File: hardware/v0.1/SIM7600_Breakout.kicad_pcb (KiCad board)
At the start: 4 copper layers, 40 x 80 mm, 68 parts, among them J1 SIM8060-6-0-14-00-A, J2 2W Header, J3 MJ-3502N, J4 30W Header, J5 2137160001, J6 U.FL-R-SMT-1(01), J7 U.FL-R-SMT-1(01), J8 U.FL-R-SMT-1(01), Q1 MMBT3904L_RFG, U1 NVT2008PW_118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

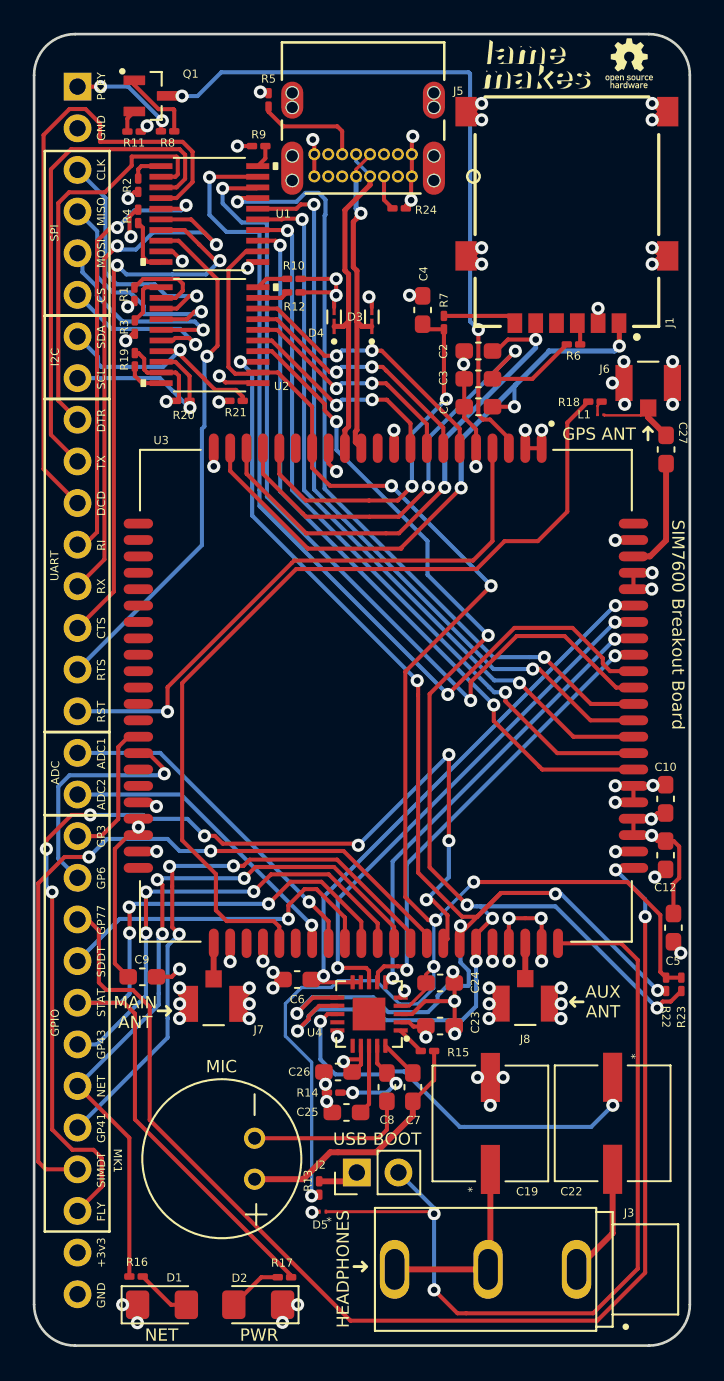
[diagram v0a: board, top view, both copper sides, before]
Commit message: Added project wide versioning, cleaned up & added PCB text
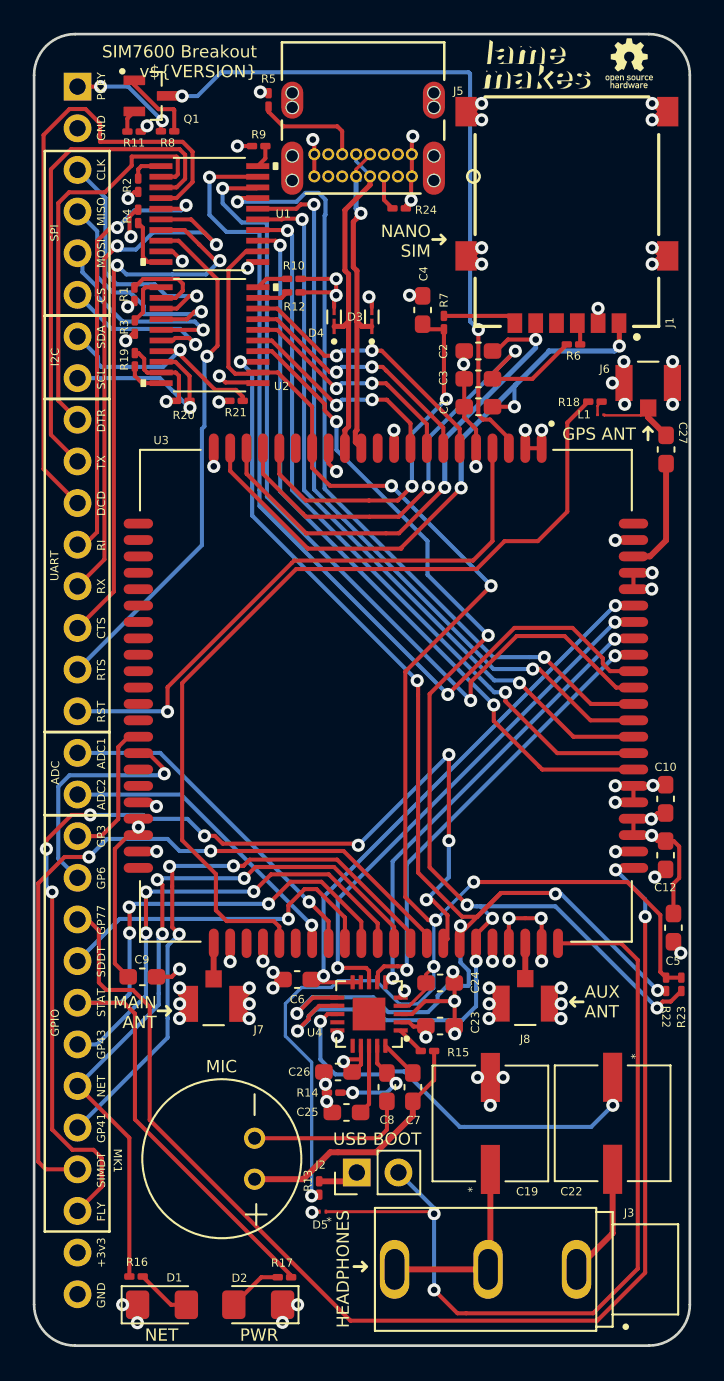
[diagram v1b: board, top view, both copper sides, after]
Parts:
- added G***: LOGO, sim7600_breakout:arrow, F.Cu at (143.7, 77.2)
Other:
- board text added: "NANO SIM"
- board text added: "SIM7600 Breakout v${VERSION}"
- board text removed: "SIM7600 Breakout Board"
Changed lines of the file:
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@@
 		)
 	)
+	(property "VERSION" "0.1")
 	(net 0 "")
 	(net 1 "/SIM_VCC")
@@
 		(at 126.13 68.44)
 		(property "Reference" "Q1"
-			(at 2.42 -1.34 0)
+			(at 2.47 1.41 0)
 			(unlocked yes)
 			(layer "F.SilkS")
@@
 		)
 	)
+	(footprint "sim7600_breakout:arrow"
+		(layer "F.Cu")
+		(at 143.7 77.2)
+		(property "Reference" "G***"
+			(at 0 -1.275 0)
+			(unlocked yes)
+			(layer "F.SilkS")
+			(hide yes)
+			(effects
+				(font
+					(size 0.5 0.5)
+					(thickness 0.075)
+				)
+			)
+		)
+		(property "Value" "LOGO"
+			(at 0.75 0 360)
+			(layer "F.SilkS")
+			(hide yes)
+			(effects
+				(font
+					(size 1.524 1.524)
+					(thickness 0.3)
+				)
+			)
+		)
+		(property "Footprint" ""
+			(at 0 0 360)
+			(layer "F.Fab")
+			(hide yes)
+			(effects
+				(font
+					(size 1.27 1.27)
+					(thickness 0.15)
+				)
+			)
+		)
+		(property "Datasheet" ""
+			(at 0 0 360)
+			(layer "F.Fab")
+			(hide yes)
+			(effects
+				(font
+					(size 1.27 1.27)
+					(thickness 0.15)
+				)
+			)
+		)
+		(property "Description" ""
+			(at 0 0 360)
+			(layer "F.Fab")
+			(hide yes)
+			(effects
+				(font
+					(size 1.27 1.27)
+					(thickness 0.15)
+				)
+			)
+		)
+		(attr board_only exclude_from_pos_files exclude_from_bom)
+		(fp_poly
+			(pts
+				(xy 0.126227 -0.360491) (xy 0.140112 -0.357103) (xy 0.153924 -0.351381) (xy 0.154416 -0.351133)
+				(xy 0.155632 -0.350501) (xy 0.156855 -0.349812) (xy 0.158161 -0.34899) (xy 0.15963 -0.34796) (xy 0.161338 -0.346647)
+				(xy 0.163363 -0.344974) (xy 0.165783 -0.342867) (xy 0.168675 -0.34025) (xy 0.172118 -0.337049) (xy 0.176189 -0.333186)
+				(xy 0.180965 -0.328588) (xy 0.186525 -0.323178) (xy 0.192946 -0.316881) (xy 0.200305 -0.309622)
+				(xy 0.208681 -0.301326) (xy 0.218152 -0.291917) (xy 0.228794 -0.281319) (xy 0.240685 -0.269457)
+				(xy 0.253904 -0.256257) (xy 0.268528 -0.241641) (xy 0.284634 -0.225536) (xy 0.302301 -0.207865)
+				(xy 0.310669 -0.199494) (xy 0.329354 -0.180805) (xy 0.346445 -0.163713) (xy 0.362015 -0.148138)
+				(xy 0.376138 -0.133999) (xy 0.388887 -0.121216) (xy 0.400338 -0.109708) (xy 0.410564 -0.099395)
+				(xy 0.41964 -0.090195) (xy 0.427638 -0.082029) (xy 0.434633 -0.074816) (xy 0.440699 -0.068476) (xy 0.445911 -0.062927)
+				(xy 0.450341 -0.058089) (xy 0.454065 -0.053882) (xy 0.457155 -0.050225) (xy 0.459687 -0.047038)
+				(xy 0.461733 -0.04424) (xy 0.463369 -0.041751) (xy 0.464668 -0.039489) (xy 0.465703 -0.037375) (xy 0.46655 -0.035327)
+				(xy 0.467282 -0.033266) (xy 0.467973 -0.031111) (xy 0.468696 -0.028781) (xy 0.469337 -0.026773)
+				(xy 0.470784 -0.021955) (xy 0.471726 -0.017603) (xy 0.47227 -0.012927) (xy 0.472524 -0.007136) (xy 0.47258 -0.002958)
+				(xy 0.472174 0.008159) (xy 0.470639 0.017989) (xy 0.467762 0.02738) (xy 0.463331 0.037177) (xy 0.461716 0.040231)
+				(xy 0.460972 0.041566) (xy 0.460162 0.042916) (xy 0.459205 0.044361) (xy 0.458026 0.045982) (xy 0.456546 0.04786)
+				(xy 0.454686 0.050074) (xy 0.452369 0.052707) (xy 0.449518 0.055838) (xy 0.446053 0.059548) (xy 0.441896 0.063919)
+				(xy 0.436971 0.06903) (xy 0.431199 0.074962) (xy 0.424501 0.081796) (xy 0.416801 0.089613) (xy 0.408019 0.098494)
+				(xy 0.398079 0.108518) (xy 0.386901 0.119767) (xy 0.374408 0.132321) (xy 0.360522 0.146262) (xy 0.345166 0.161669)
+				(xy 0.32826 0.178624) (xy 0.317759 0.189153) (xy 0.302534 0.204411) (xy 0.287675 0.219289) (xy 0.273275 0.233694)
+				(xy 0.259428 0.247531) (xy 0.246229 0.260708) (xy 0.233772 0.27313) (xy 0.22215 0.284704) (xy 0.211457 0.295337)
+				(xy 0.201789 0.304935) (xy 0.193238 0.313404) (xy 0.1859 0.320651) (xy 0.179867 0.326583) (xy 0.175235 0.331104)
+				(xy 0.172097 0.334123) (xy 0.170663 0.335448) (xy 0.158717 0.344247) (xy 0.145694 0.350941) (xy 0.137851 0.353793)
+				(xy 0.130727 0.355448) (xy 0.122255 0.356524) (xy 0.113296 0.356981) (xy 0.104711 0.356781) (xy 0.097363 0.355886)
+				(xy 0.096277 0.355657) (xy 0.082291 0.351348) (xy 0.069609 0.34508) (xy 0.058132 0.336798) (xy 0.052745 0.331817)
+				(xy 0.043545 0.321006) (xy 0.03636 0.309102) (xy 0.031255 0.296339) (xy 0.028294 0.282948) (xy 0.027541 0.269165)
+				(xy 0.029062 0.255223) (xy 0.030166 0.250261) (xy 0.031498 0.246038) (xy 0.033581 0.240597) (xy 0.036068 0.234814)
+				(xy 0.037426 0.23192) (xy 0.042891 0.220679) (xy 0.111031 0.152359) (xy 0.179171 0.08404) (xy -0.111274 0.08373)
+				(xy -0.142293 0.083696) (xy -0.171034 0.083663) (xy -0.197587 0.08363) (xy -0.22204 0.083597) (xy -0.244483 0.083562)
+				(xy -0.265005 0.083524) (xy -0.283695 0.083484) (xy -0.300641 0.083441) (xy -0.315934 0.083393)
+				(xy -0.329661 0.08334) (xy -0.341913 0.083281) (xy -0.352778 0.083216) (xy -0.362344 0.083143) (xy -0.370702 0.083063)
+				(xy -0.377941 0.082974) (xy -0.384148 0.082875) (xy -0.389414 0.082767) (xy -0.393828 0.082647)
+				(xy -0.397478 0.082517) (xy -0.400453 0.082373) (xy -0.402844 0.082217) (xy -0.404738 0.082047)
+				(xy -0.406224 0.081863) (xy -0.407393 0.081663) (xy -0.408332 0.081448) (xy -0.408818 0.081312)
+				(xy -0.422421 0.076106) (xy -0.434791 0.069016) (xy -0.445756 0.060216) (xy -0.455142 0.049881)
+				(xy -0.462778 0.038185) (xy -0.468491 0.025303) (xy -0.470451 0.018932) (xy -0.471744 0.011974)
+				(xy -0.47244 0.003619) (xy -0.472536 -0.005262) (xy -0.472029 -0.013794) (xy -0.470917 -0.021107)
+				(xy -0.470586 -0.022482) (xy -0.469144 -0.02699) (xy -0.466955 -0.032666) (xy -0.464387 -0.038593)
+				(xy -0.463051 -0.041412) (xy -0.456158 -0.052813) (xy -0.44737 -0.063021) (xy -0.43694 -0.07183)
+				(xy -0.425126 -0.079032) (xy -0.412183 -0.084421) (xy -0.408647 -0.085504) (xy -0.399352 -0.088145)
+				(xy -0.110102 -0.088471) (xy 0.179149 -0.088796) (xy 0.110473 -0.157696) (xy 0.098167 -0.170043)
+				(xy 0.087419 -0.180837) (xy 0.078113 -0.1902) (xy 0.070136 -0.198254) (xy 0.063375 -0.205122) (xy 0.057714 -0.210926)
+				(xy 0.053041 -0.215788) (xy 0.04924 -0.219832) (xy 0.046199 -0.223178) (xy 0.043803 -0.225951) (xy 0.041938 -0.228271)
+				(xy 0.04049 -0.230262) (xy 0.039346 -0.232045) (xy 0.038391 -0.233744) (xy 0.03751 -0.235481) (xy 0.036941 -0.236654)
+				(xy 0.031432 -0.250464) (xy 0.028283 -0.264219) (xy 0.02749 -0.277976) (xy 0.029049 -0.291793) (xy 0.032509 -0.304468)
+				(xy 0.037902 -0.316484) (xy 0.045301 -0.32765) (xy 0.054412 -0.337674) (xy 0.06494 -0.346262) (xy 0.076591 -0.353122)
+				(xy 0.084866 -0.356601) (xy 0.098531 -0.360246) (xy 0.112342 -0.361541)
+			)
+			(stroke
+				(width 0)
+				(type solid)
+			)
+			(fill solid)
+			(layer "F.SilkS")
+		)
+	)
 	(footprint "Resistor_SMD:R_0201_0603Metric_Pad0.64x0.40mm_HandSolder"
 		(layer "F.Cu")
@@
 		)
 	)
-	(gr_text "SIM7600 Breakout Board"
-		(at 158.275 100.7 270)
+	(gr_text "NANO\nSIM"
+		(at 143.2 77.3 0)
+		(layer "F.SilkS")
+		(effects
+			(font
+				(size 0.75 0.75)
+				(thickness 0.15)
+			)
+			(justify right)
+		)
+	)
+	(gr_text "SIM7600 Breakout\nv${VERSION}"
+		(at 132.6 66.35 0)
 		(layer "F.SilkS")
 		(effects
@@
 				(thickness 0.15)
 			)
+			(justify right)
 		)
 	)
@@
 	)
 	(gr_text "MAIN\nANT"
-		(at 125.175 124.35 0)
+		(at 126.481509 124.35 0)
 		(layer "F.SilkS")
 		(effects
@@
 				(thickness 0.15)
 			)
+			(justify right)
 		)
 	)
@@
 	)
 	(gr_text "AUX\nANT"
-		(at 153.7 123.7 0)
+		(at 152.57244 123.7 0)
 		(layer "F.SilkS")
 		(effects
@@
 				(thickness 0.15)
 			)
+			(justify left)
 		)
 	)
